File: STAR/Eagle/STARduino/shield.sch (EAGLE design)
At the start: 54 parts, among them J1 J30J-9J30J, U1 PCA9515A, U10 PCA9306DCT, U11 CC2, U12 SSCMNNN015PA2A3, U2 ATSAMD21G18, U3 MAX31725MTA+, U4 MC74VHC1GT125, U5 DS3231MZ+, U6 MC14504BDTG, U7 BMX055, U8 ADXL375BCCZ, U9 TCA9535_RTW_24

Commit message: starduino shield for M0 becuase custom boards don't always work
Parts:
- removed C1, C2, C3, C4, C7, C8: 100nF, resistor:C-USC0603
- removed C10, C11: 6.8pF, resistor:C-USC0603
- removed C19: 100pF, rcl:C-USC0603
- removed C5: 1uF, resistor:C-USC0603
- removed C6: 10uF, resistor:C-USC0603
- removed FB1, FB2: BLM18KG221BH1D, AR_passives:FERRITE_BEAD-0603
- removed IMAG1: SSL.3IN_SILK, images:SSL.3IN_SILK
- removed J1: J30J-9J30J, CM_J30J:J30J-9J30J
- removed JP1: (no value), pinhead:PINHD-2X5
- removed JP2: (no value), CM_passives:JUMPER-2PTH
- removed R1, R2: 10k, resistor:R-US_R0603
- removed R10, R9: 4.7k, rcl:R-US_R0603
- removed R3: 4.7k, resistor:R-US_R0603
- removed R4: 330, resistor:R-US_R0603
- removed R5: 3.6k, resistor:R-US_R0603
- removed R6: 6.8k, resistor:R-US_R0603
- removed R8: 220k, rcl:R-US_R0603
- removed U10: PCA9306DCT, MotorDriver:PCA9306DCT
- removed U2: ATSAMD21G18, AR_mcu:ATSAMD21G18
- removed U4: MC74VHC1GT125, CM_IC:MC74VHC1GT125
- removed U6: MC14504BDTG, MotorDriver:MC14504BDTG
- removed U9: TCA9535_RTW_24, MotorDriver:TCA9535_RTW_24
- removed XTAL1: ABS07AIG-32.768KHZ-1-T, AR_XTAL:ABS07AIG-32.768KHZ-1-T
- added AD: 6x1F-H8.5, SmartPrj:PINHD-1X6
- added IOH: 10x1F-H8.5, SmartPrj:PINHD-1X10_ARD
- added IOL, POWER: 8x1F-H8.5, SmartPrj:PINHD-1X8
- added R11: 4.7k, SparkFun-Passives:RESISTOR-ARRAY0603-ARV
- added U$2: SSLORIG, images:SSLORIG
- added U$3: FODM8061-D, optoisolater:FODM8061-D
- R7: device SparkFun-Passives:RESISTOR-ARRAY0603-ARV -> resistor:R-US_R0603
- U$1: value FODM8061-D -> BALLOON; device optoisolater:FODM8061-D -> images:BALLOON
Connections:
- removed net 5V_S: R10.2, R5.1, R8.2, R9.2, U6.VDD, U9.A0, U9.A1, U9.A2, U9.VCC
- removed net IMUDR: U6.DIN, U7.DRDYM
- removed net IMUINT1: U6.BIN, U7.INT1
- removed net IMUINT2: U6.CIN, U7.INT2
- removed net IMUINT3: U6.AIN, U7.INT3
- removed net IMUINT4: U6.EIN, U7.INT4
- removed net IMUINT5: U6.FIN, U7.INT5
- removed net IOEINT: U2.PA17/I2C/EIC/SCOM1PAD1+/TC2, U4.Y
- removed net MISO: J1.2, U2.PA12/I2C/EIC/SCOM2PAD0+/TC2
- removed net MOSI: J1.1, U2.PB10/EIC/SCOM4PAD2/TC5
- removed net N$10: C6.1, C7.1, FB2.P$2, U2.VDDANA
- removed net N$19: U6.AOUT, U9.P00
- removed net N$23: U6.BOUT, U9.P01
- removed net N$25: U4.A, U9.INT
- removed net N$28: U6.COUT, U9.P02
- removed net N$29: U6.DOUT, U9.P03
- removed net N$31 (its old number): U6.FOUT, U9.P05
- removed net N$33: R10.1, U10.SDA2, U9.SDA
- removed net N$34: R9.1, U10.SCL2, U9.SCL
- removed net N$35: C19.1, R8.1, U10.EN, U10.VREF2
- removed net N$5: C5.1, U2.VDDCORE
- removed net N$6: R3.1, U3.OS
- removed net N$7: JP2.2, R4.1
- removed net PA27: U2.PA27/EIC, U5.!INT!/SQW
- removed net PB02: U2.PB02/EIC/AIN10/SCOM5PAD0, U8.INT1
- removed net PB03: U2.PB03/EIC/AIN11/SCOM5PAD1, U8.INT2
- removed net SCK: J1.3, U2.PB11/EIC/SCOM4PAD3/TC5
- removed net SWDCLK: JP1.4, R1.1, U2.PA30/EIC/SCOM1PAD2/SWDCLK
- removed net SWDIO: JP1.2, U2.PA31/EIC/SCOM1PAD3/SWDIO
- removed net VREFA: C1.1, FB1.P$1, U2.PA03/EIC/REF/AI/VREFA
- removed net V_SENSE: R5.2, R6.1, U2.PA02/EIC/AIN
- removed net XIN32: C10.1, U2.PA00/XIN32/EIC/SCOM1PAD0, XTAL1.2
- removed net XOUT32: C11.1, U2.PA01/XOUT32/EIC/SCOM1PAD1, XTAL1.1
- new net +5V: POWER.5
- new net A0: AD.1
- new net A1: AD.2
- new net A2: AD.3
- new net A3\: AD.4
- new net A4: AD.5
- new net A5: AD.6
- new net AREF: IOH.8
- new net D1: IOL.2
- new net D10: IOH.3
- new net D11: IOH.4
- new net D12: IOH.5
- new net D13: IOH.6
- new net D2: IOL.3
- new net D3: IOL.4
- new net D4: IOL.5
- new net D5: IOL.6
- new net D6: IOL.7
- new net D7: IOL.8
- new net D8: IOH.1
- new net D9: IOH.2
- new net IOREF: POWER.2
- new net N$52: POWER.1
- new net VIN: POWER.8
- net +3V3: now also POWER.4, R11A.2, R11B.2, R11C.2, R11D.2, R7.2; no longer C2.1, C3.1, C4.1, FB1.P$2, FB2.P$1, J1.6, J1.8, JP1.1, R1.2, R2.2, R3.2, R7A.2, R7B.2, R7C.2, R7D.2, U10.VREF1, U2.VCC, U2.VDDIO1, U2.VDDIO2, U4.VIN, U6.VCC
- net BIAS_REF: no longer U2.PB08/EIC/AIN2/SCOM4PAD0/TC4
- net GND: now also IOH.7, POWER.6, POWER.7, U$3.CAT; no longer C1.2, C10.2, C11.2, C19.2, C2.2, C3.2, C4.2, C5.2, C6.2, C7.2, C8.2, J1.5, J1.7, JP1.3, JP1.5, JP2.1, R6.2, U$1.CAT, U10.GND, U2.GND1, U2.GND2, U2.GND3, U2.GNDANA, U4.GND, U4.OE, U6.MODE, U6.VSS, U9.EPAD, U9.GND
- net MOTOR: now also IOL.1, U$3.AN; no longer U$1.AN, U2.PA05/EIC/AIN5/SCOM0PAD1
- net MOTOR_GND: now also U$3.GND; no longer U$1.GND
- net MOTOR_SIGNAL: now also U$3.VO; no longer U$1.VO
- net MOTOR_VCC: now also U$3.VCC; no longer U$1.VCC
- net N$30: now also R7.1, U3.OS; no longer U6.EOUT, U9.P04
- net RESET: now also POWER.3; no longer C8.1, JP1.10, R2.1, R4.2, U2.RESET
- net SCL: now also IOH.10, R11C.1; no longer R7C.1, U10.SCL1, U2.PA23/I2C/EIC/SCOM5PAD1+/TC4
- net SCL_BUFF: now also R11B.1; no longer R7B.1
- net SDA: now also IOH.9, R11D.1; no longer R7D.1, U10.SDA1, U2.PA22/I2C/EIC/SCOM5PAD0+/TC4
- net SDA_BUFF: now also R11A.1; no longer R7A.1
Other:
- note added: "0"
- note added: "1"
- note added: "2"
- note added: "3"
- note added: "4"
- note added: "5"
- note added: "6"
- note added: "7"
- note removed: "AREF"
- note removed: "Cortex Debug Connector"
- note removed: "MICROCONTROLLER BLOCK"
- note removed: "MULTIPLEXER"
- note removed: "RESET SWITCH"
- note removed: "V SENSE"
- note removed: "XTAL"

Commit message: Fixed optoisolator circuit and added SPI header on top, but not yet the SPI head on the ICSP board. Fixed a lot of air wires
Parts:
- removed U1: PCA9515A, CM_IC:PCA9515A
- added C1: 100nF, resistor:C-USC0603
- added C2: 15pf, resistor:C-USC0603
- added JP1: (no value), pinhead:PINHD-1X5
- added R1, R2: 442, resistor:R-US_R0603
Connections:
- removed net A2: AD.3
- removed net SCL_BUFF: R11B.1, U1.SCL1
- removed net SDA_BUFF: R11A.1, U1.SDA1
- new net MISO: JP1.3
- new net MOSI: JP1.4
- new net N$2: R2.1, U$3.AN
- new net SCK: JP1.5
- net +3V3: now also JP1.1; no longer R11A.2, R11B.2, U1.VCC
- net BIAS_REF: now also AD.3
- net GND: now also JP1.2; no longer U1.GND
- net MOTOR: now also R2.2; no longer U$3.AN
- net MOTOR_GND: now also C1.2, C2.2
- net MOTOR_SIGNAL: now also C2.1, R1.2
- net MOTOR_VCC: now also C1.1, R1.1
- net SCL: no longer U1.SCL0
- net SDA: no longer U1.SDA0
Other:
- moved on the sheet: C20

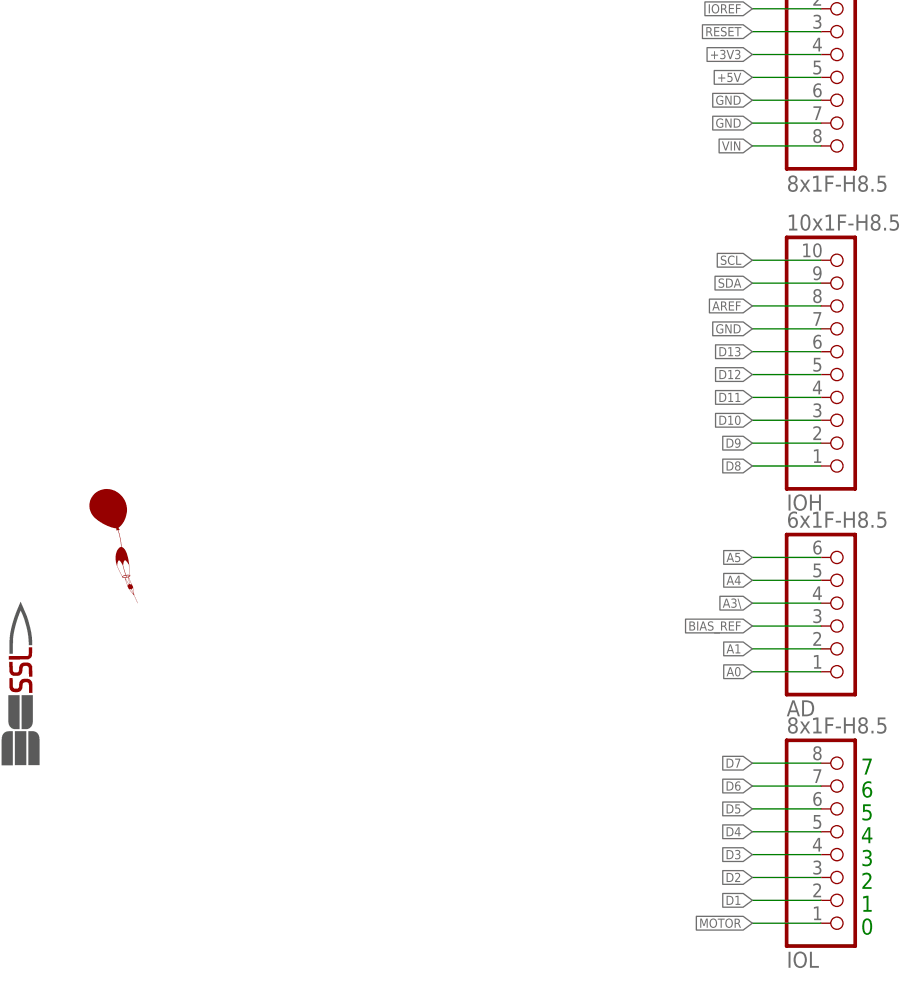
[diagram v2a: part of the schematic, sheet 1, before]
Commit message: Added ICSP header and finished reviewing starduino
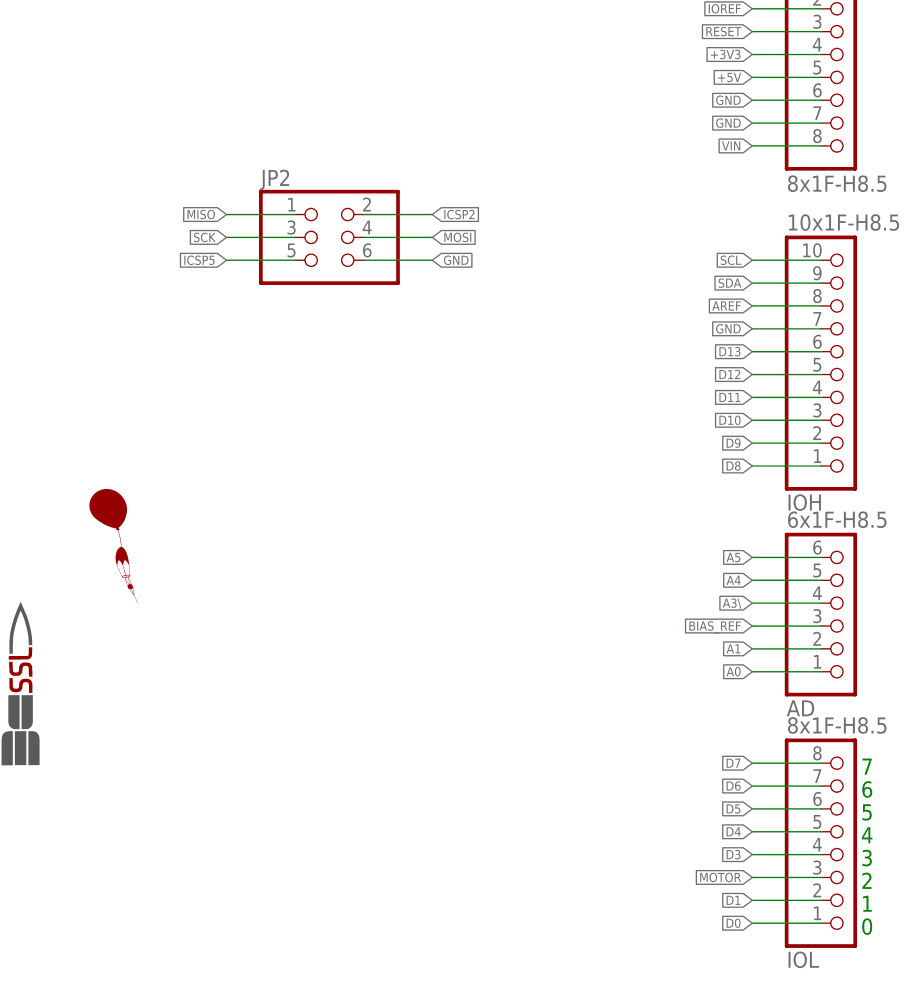
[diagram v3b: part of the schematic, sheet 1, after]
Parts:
- added JP2: (no value), pinhead:PINHD-2X3
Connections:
- removed net D2: IOL.3
- new net D0: IOL.1
- new net ICSP2: JP2.2
- new net ICSP5: JP2.5
- net GND: now also JP2.6
- net MISO: now also JP2.1
- net MOSI: now also JP2.4
- net MOTOR: now also IOL.3; no longer IOL.1
- net SCK: now also JP2.3
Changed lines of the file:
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@@
 <part name="C2" library="resistor" deviceset="C-US" device="C0603" value="15pf"/>
 <part name="JP1" library="pinhead" library_urn="urn:adsk.eagle:library:325" deviceset="PINHD-1X5" device="" package3d_urn="urn:adsk.eagle:package:22469/2"/>
+<part name="JP2" library="pinhead" library_urn="urn:adsk.eagle:library:325" deviceset="PINHD-2X3" device="" package3d_urn="urn:adsk.eagle:package:22462/2"/>
 </parts>
 <sheets>
@@
 <instance part="U$1" gate="G$1" x="139.7" y="58.42"/>
 <instance part="U$2" gate="G$1" x="132.08" y="48.26"/>
+<instance part="JP2" gate="A" x="165.1" y="99.06"/>
 </instances>
 <busses>
@@
 </segment>
 </net>
-<net name="D2" class="0">
+<net name="MOTOR" class="0">
 <segment>
 <pinref part="IOL" gate="A" pin="3"/>
@@
 </segment>
 </net>
-<net name="MOTOR" class="0">
-<segment>
-<pinref part="IOL" gate="A" pin="1"/>
-<wire x1="220.98" y1="22.86" x2="213.36" y2="22.86" width="0.1524" layer="91"/>
-<label x="213.36" y="22.86" size="1.016" layer="95" rot="R180" xref="yes"/>
-</segment>
-</net>
 <net name="D5" class="0">
 <segment>
@@
 <label x="213.36" y="88.9" size="1.016" layer="95" rot="R180" xref="yes"/>
 </segment>
+<segment>
+<pinref part="JP2" gate="A" pin="6"/>
+<wire x1="170.18" y1="96.52" x2="177.8" y2="96.52" width="0.1524" layer="91"/>
+<label x="177.8" y="96.52" size="1.016" layer="95" xref="yes"/>
+</segment>
 </net>
 <net name="+5V" class="0">
@@
 </segment>
 </net>
+<net name="MISO" class="0">
+<segment>
+<pinref part="JP2" gate="A" pin="1"/>
+<wire x1="162.56" y1="101.6" x2="154.94" y2="101.6" width="0.1524" layer="91"/>
+<label x="154.94" y="101.6" size="1.016" layer="95" rot="MR0" xref="yes"/>
+</segment>
+</net>
+<net name="SCK" class="0">
+<segment>
+<pinref part="JP2" gate="A" pin="3"/>
+<wire x1="162.56" y1="99.06" x2="154.94" y2="99.06" width="0.1524" layer="91"/>
+<label x="154.94" y="99.06" size="1.016" layer="95" rot="MR0" xref="yes"/>
+</segment>
+</net>
+<net name="ICSP5" class="0">
+<segment>
+<pinref part="JP2" gate="A" pin="5"/>
+<wire x1="162.56" y1="96.52" x2="154.94" y2="96.52" width="0.1524" layer="91"/>
+<label x="154.94" y="96.52" size="1.016" layer="95" rot="MR0" xref="yes"/>
+</segment>
+</net>
+<net name="ICSP2" class="0">
+<segment>
+<pinref part="JP2" gate="A" pin="2"/>
+<wire x1="170.18" y1="101.6" x2="177.8" y2="101.6" width="0.1524" layer="91"/>
+<label x="177.8" y="101.6" size="1.016" layer="95" xref="yes"/>
+</segment>
+</net>
+<net name="MOSI" class="0">
+<segment>
+<pinref part="JP2" gate="A" pin="4"/>
+<wire x1="170.18" y1="99.06" x2="177.8" y2="99.06" width="0.1524" layer="91"/>
+<label x="177.8" y="99.06" size="1.016" layer="95" xref="yes"/>
+</segment>
+</net>
+<net name="D0" class="0">
+<segment>
+<pinref part="IOL" gate="A" pin="1"/>
+<wire x1="220.98" y1="22.86" x2="213.36" y2="22.86" width="0.1524" layer="91"/>
+<label x="213.36" y="22.86" size="1.016" layer="95" rot="MR0" xref="yes"/>
+</segment>
+</net>

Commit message: STARduino sheild. Updated holes, resistor size, added some names to components to make assembly easier
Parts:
- R1, R2: device resistor:R-US_R0603 -> resistor:R-US_R0805
- renumbered U$3 to MOTORDRIVER, U11 to CC2, U3 to MAX31725MTA+, U5 to DS3231MZ+, U7 to BMX055, U8 to ADXL375BCCZ
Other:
- moved on the sheet: C1
